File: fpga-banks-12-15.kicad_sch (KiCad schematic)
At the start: 1 part, among them U15 XC7K160T-FFG676

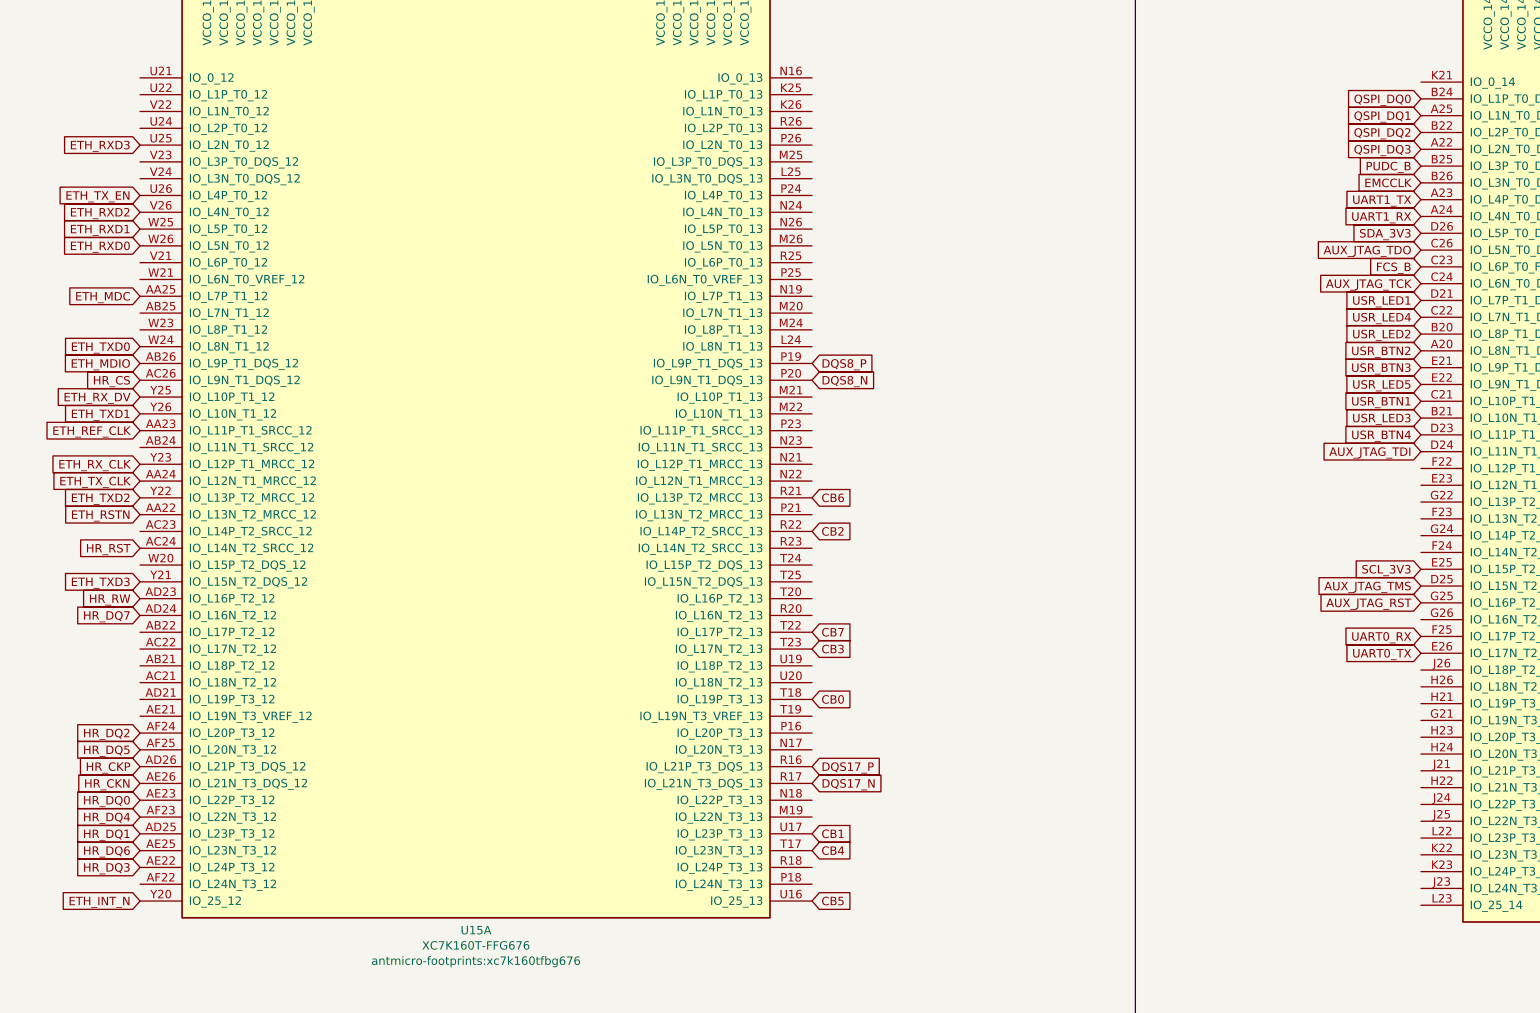
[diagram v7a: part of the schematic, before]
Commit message: Assign and connect misc. signals. Add, place and route decoupling capacitors
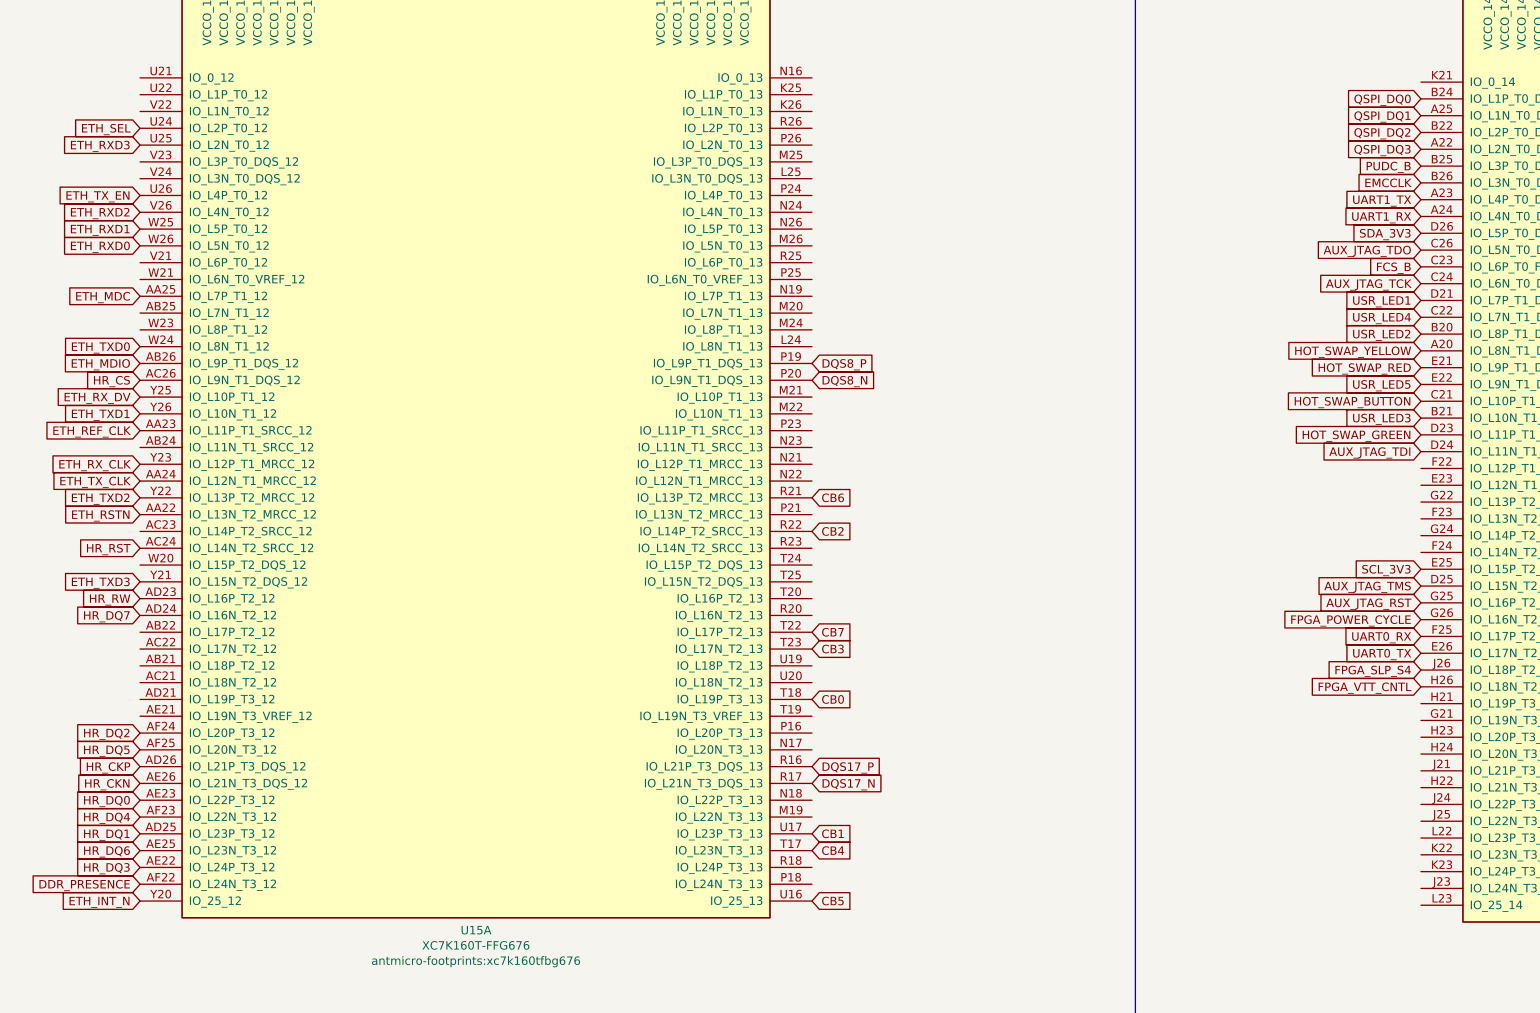
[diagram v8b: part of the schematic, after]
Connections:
- net DDR_PRESENCE: now reaches U15.AF22 (IO_L24N_T3_12)
- net ETH_SEL: now reaches U15.U24 (IO_L2P_T0_12)
- net FPGA_POWER_CYCLE: now reaches U15.G26 (IO_L16N_T2_A15_D31_14)
- net FPGA_VTT_CNTL: now reaches U15.H26 (IO_L18N_T2_A11_D27_14)
- net FPGA_SLP_S4: now reaches U15.J26 (IO_L18P_T2_A12_D28_14)
- net USR_BTN1 renamed HOT_SWAP_BUTTON
- net USR_BTN2 renamed HOT_SWAP_YELLOW
- net USR_BTN3 renamed HOT_SWAP_RED
- net USR_BTN4 renamed HOT_SWAP_GREEN
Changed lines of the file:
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@@
+    )
+  )
+  (global_label "FPGA_SLP_S4" (shape input) (at 253.365 181.61 180) (fields_autoplaced)
+    (effects (font (size 1.27 1.27)) (justify right))
+    (property "Intersheet References" "${INTERSHEET_REFS}" (id 0) (at 238.4618 181.5306 0)
+      (effects (font (size 1.27 1.27)) (justify right) hide)
     )
   )
@@
     )
   )
+  (global_label "HOT_SWAP_GREEN" (shape input) (at 253.365 146.05 180) (fields_autoplaced)
+    (effects (font (size 1.27 1.27)) (justify right))
+    (property "Intersheet References" "${INTERSHEET_REFS}" (id 0) (at 234.2889 145.9706 0)
+      (effects (font (size 1.27 1.27)) (justify right) hide)
+    )
+  )
   (global_label "HR_CKP" (shape input) (at 59.69 196.215 180) (fields_autoplaced)
     (effects (font (size 1.27 1.27)) (justify right))
@@
     )
   )
+  (global_label "DDR_PRESENCE" (shape input) (at 59.69 213.995 180) (fields_autoplaced)
+    (effects (font (size 1.27 1.27)) (justify right))
+    (property "Intersheet References" "${INTERSHEET_REFS}" (id 0) (at 42.791 213.9156 0)
+      (effects (font (size 1.27 1.27)) (justify right) hide)
+    )
+  )
   (global_label "HR_DQ5" (shape input) (at 59.69 193.675 180) (fields_autoplaced)
     (effects (font (size 1.27 1.27)) (justify right))
@@
     )
   )
+  (global_label "FPGA_VTT_CNTL" (shape input) (at 253.365 184.15 180) (fields_autoplaced)
+    (effects (font (size 1.27 1.27)) (justify right))
+    (property "Intersheet References" "${INTERSHEET_REFS}" (id 0) (at 236.7684 184.0706 0)
+      (effects (font (size 1.27 1.27)) (justify right) hide)
+    )
+  )
   (global_label "HR_DQ3" (shape input) (at 59.69 211.455 180) (fields_autoplaced)
     (effects (font (size 1.27 1.27)) (justify right))
@@
     )
   )
+  (global_label "HOT_SWAP_BUTTON" (shape input) (at 253.365 140.97 180) (fields_autoplaced)
+    (effects (font (size 1.27 1.27)) (justify right))
+    (property "Intersheet References" "${INTERSHEET_REFS}" (id 0) (at 233.2608 141.0494 0)
+      (effects (font (size 1.27 1.27)) (justify right) hide)
+    )
+  )
   (global_label "FMC_IO_10_N" (shape input) (at 354.965 143.51 0) (fields_autoplaced)
     (effects (font (size 1.27 1.27)) (justify left))
@@
     )
   )
+  (global_label "HOT_SWAP_RED" (shape input) (at 253.365 135.89 180) (fields_autoplaced)
+    (effects (font (size 1.27 1.27)) (justify right))
+    (property "Intersheet References" "${INTERSHEET_REFS}" (id 0) (at 236.7684 135.8106 0)
+      (effects (font (size 1.27 1.27)) (justify right) hide)
+    )
+  )
   (global_label "DQS8_N" (shape input) (at 161.29 137.795 0) (fields_autoplaced)
     (effects (font (size 1.27 1.27)) (justify left))
@@
     )
   )
-  (global_label "USR_BTN2" (shape input) (at 253.365 133.35 180) (fields_autoplaced)
-    (effects (font (size 1.27 1.27)) (justify right))
-    (property "Intersheet References" "${INTERSHEET_REFS}" (id 0) (at 0 0 0)
-      (effects (font (size 1.27 1.27)) hide)
+  (global_label "FPGA_POWER_CYCLE" (shape input) (at 253.365 173.99 180) (fields_autoplaced)
+    (effects (font (size 1.27 1.27)) (justify right))
+    (property "Intersheet References" "${INTERSHEET_REFS}" (id 0) (at 232.1118 173.9106 0)
+      (effects (font (size 1.27 1.27)) (justify right) hide)
     )
   )
@@
     )
   )
-  (global_label "USR_BTN1" (shape input) (at 253.365 140.97 180) (fields_autoplaced)
-    (effects (font (size 1.27 1.27)) (justify right))
-    (property "Intersheet References" "${INTERSHEET_REFS}" (id 0) (at 0 0 0)
-      (effects (font (size 1.27 1.27)) hide)
-    )
-  )
   (global_label "ETH_TXD3" (shape input) (at 59.69 168.275 180) (fields_autoplaced)
     (effects (font (size 1.27 1.27)) (justify right))
@@
     )
   )
+  (global_label "ETH_SEL" (shape input) (at 59.69 99.695 180) (fields_autoplaced)
+    (effects (font (size 1.27 1.27)) (justify right))
+    (property "Intersheet References" "${INTERSHEET_REFS}" (id 0) (at 49.5644 99.6156 0)
+      (effects (font (size 1.27 1.27)) (justify right) hide)
+    )
+  )
   (global_label "ETH_RX_CLK" (shape input) (at 59.69 150.495 180) (fields_autoplaced)
     (effects (font (size 1.27 1.27)) (justify right))
@@
     )
   )
-  (global_label "USR_BTN3" (shape input) (at 253.365 135.89 180) (fields_autoplaced)
-    (effects (font (size 1.27 1.27)) (justify right))
-    (property "Intersheet References" "${INTERSHEET_REFS}" (id 0) (at 0 0 0)
-      (effects (font (size 1.27 1.27)) hide)
-    )
-  )
-  (global_label "USR_BTN4" (shape input) (at 253.365 146.05 180) (fields_autoplaced)
-    (effects (font (size 1.27 1.27)) (justify right))
-    (property "Intersheet References" "${INTERSHEET_REFS}" (id 0) (at 0 0 0)
-      (effects (font (size 1.27 1.27)) hide)
-    )
-  )
   (global_label "FCS_B" (shape input) (at 253.365 120.65 180) (fields_autoplaced)
     (effects (font (size 1.27 1.27)) (justify right))
@@
     )
   )
+  (global_label "HOT_SWAP_YELLOW" (shape input) (at 253.365 133.35 180) (fields_autoplaced)
+    (effects (font (size 1.27 1.27)) (justify right))
+    (property "Intersheet References" "${INTERSHEET_REFS}" (id 0) (at 233.3818 133.2706 0)
+      (effects (font (size 1.27 1.27)) (justify right) hide)
+    )
+  )
